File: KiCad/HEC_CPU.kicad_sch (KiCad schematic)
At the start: 19 parts, among them J3 Conn_02x05_Odd_Even, SW2 SW_Push, U1 Z80CPU, U16 74LS32, U20 74LS574, U21 74LS574, U22 74LS02, U23 74LS74, U34 74LS393, U36 74LS574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

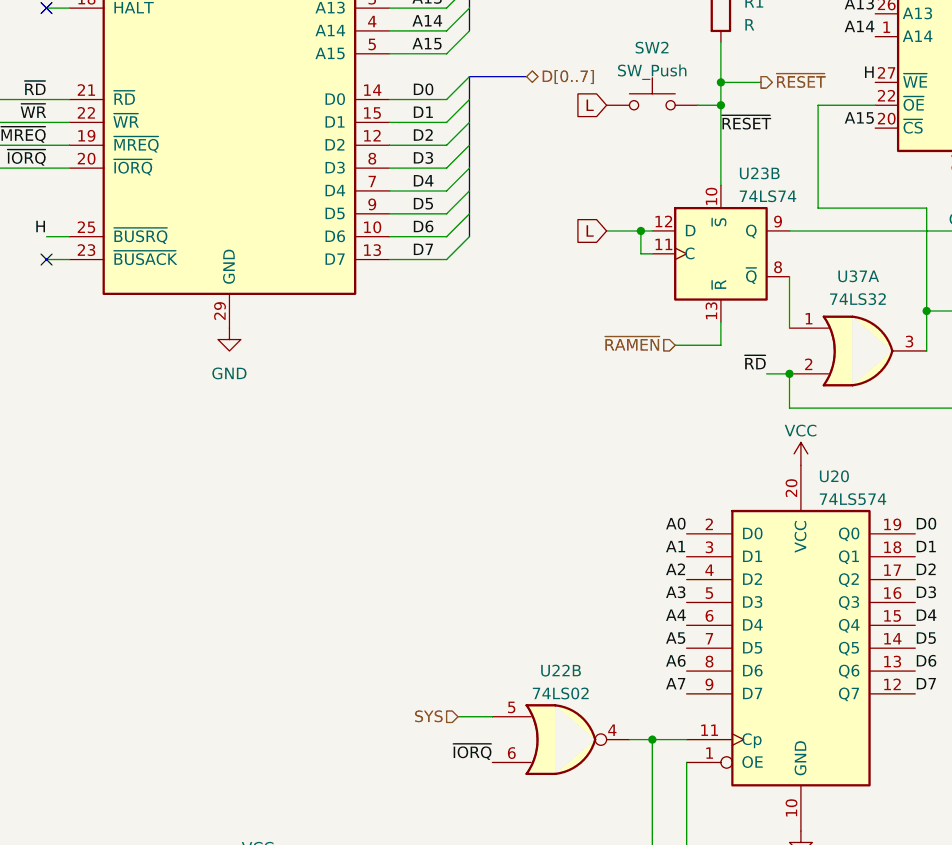
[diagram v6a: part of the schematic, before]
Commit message: Updated layout
Updated the layout of PCB. Chips on the board in this version might be in their final position.
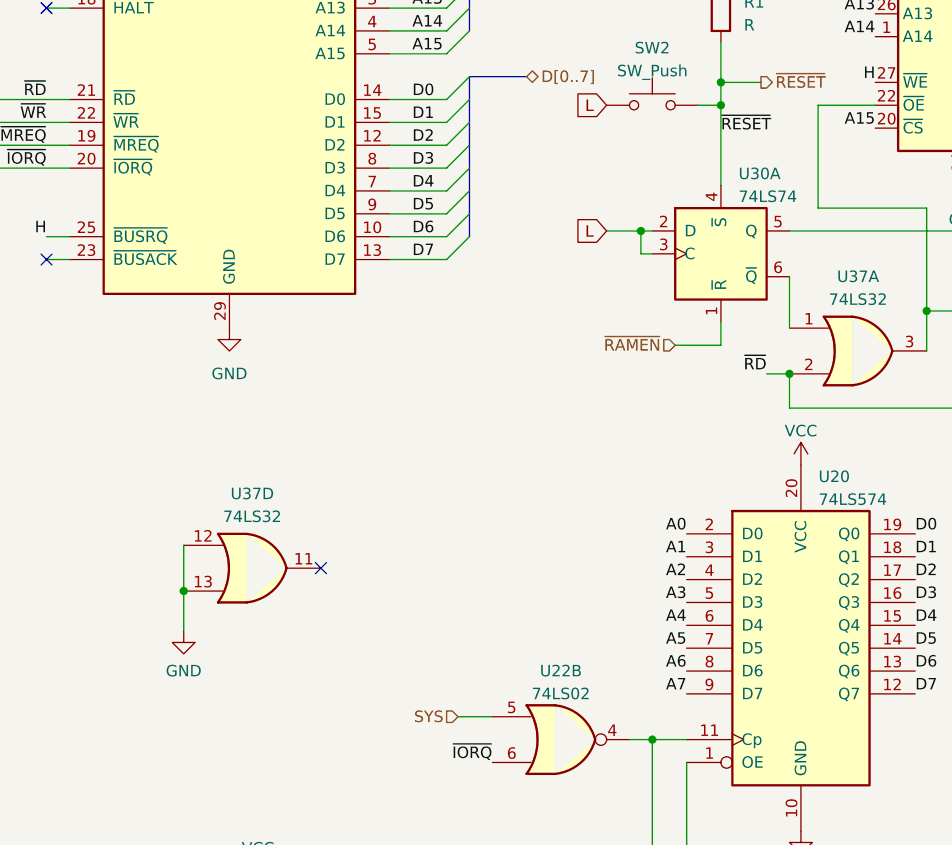
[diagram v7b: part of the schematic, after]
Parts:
- removed U23: 74LS74, Package_DIP:DIP-14_W7.62mm_Socket, symbol 74xx:74LS74
- added U30: 74LS74, Package_DIP:DIP-14_W7.62mm_Socket, symbol 74xx:74LS74
- added unit 4 of U37
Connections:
- net GND: now also U37.12, U37.13
- net L: now also U30.2 (D), U30.3 (C)
- net ~{RAMEN}: now also U30.1 (~{R})
- net ~{RESET}: now also U30.4 (~{S})
- net at U37.1: now also U30.6 (~{Q})
- net at U37.4: now also U30.5 (Q)
- no-connect marks 4 -> 5
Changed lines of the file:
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@@
   (junction (at 101.6 67.945) (diameter 0) (color 0 0 0 0)
+  )
+  (junction (at 41.91 121.92) (diameter 0) (color 0 0 0 0)
   )
   (junction (at 92.71 81.915) (diameter 0) (color 0 0 0 0)
@@
   (no_connect (at 26.67 85.09))
   (no_connect (at 192.405 40.64))
+  (no_connect (at 57.15 119.38))
   (bus_entry (at 71.12 62.23) (size 2.54 -2.54)
     (stroke (width 0) (type default))
@@
     (stroke (width 0) (type default))
   )
+  (wire (pts (xy 41.91 116.84) (xy 41.91 121.92))
+    (stroke (width 0) (type default))
+  )
   (wire (pts (xy 101.6 65.405) (xy 106.045 65.405))
     (stroke (width 0) (type default))
@@
   )
   (wire (pts (xy 280.67 30.48) (xy 278.13 30.48))
+    (stroke (width 0) (type default))
+  )
+  (wire (pts (xy 41.91 121.92) (xy 41.91 126.365))
     (stroke (width 0) (type default))
   )
@@
         (path "/87935374-b60a-4f41-99da-94b76103dd77/73a0c68b-1e42-4c0d-ae31-b1a96d0648bb"
           (reference "#PWR027") (unit 1)
+        )
+      )
+    )
+  )
+  (symbol (lib_id "74xx:74LS32") (at 49.53 119.38 0) (unit 4)
+    (in_bom yes) (on_board yes) (dnp no) (fields_autoplaced)
+    (property "Reference" "U37" (at 49.53 111.125 0)
+      (effects (font (size 1.27 1.27)))
+    )
+    (property "Value" "74LS32" (at 49.53 113.665 0)
+      (effects (font (size 1.27 1.27)))
+    )
+    (property "Footprint" "Package_DIP:DIP-14_W7.62mm_Socket" (at 49.53 119.38 0)
+      (effects (font (size 1.27 1.27)) hide)
+    )
+    (property "Datasheet" "http://www.ti.com/lit/gpn/sn74LS32" (at 49.53 119.38 0)
+      (effects (font (size 1.27 1.27)) hide)
+    )
+    (pin "1")
+    (pin "2")
+    (pin "3")
+    (pin "4")
+    (pin "5")
+    (pin "6")
+    (pin "10")
+    (pin "8")
+    (pin "9")
+    (pin "11")
+    (pin "12")
+    (pin "13")
+    (pin "14")
+    (pin "7")
+    (instances
+      (project "HEC1"
+        (path "/87935374-b60a-4f41-99da-94b76103dd77/73a0c68b-1e42-4c0d-ae31-b1a96d0648bb"
+          (reference "U37") (unit 4)
+        )
+        (path "/87935374-b60a-4f41-99da-94b76103dd77"
+          (reference "U37") (unit 4)
+        )
+        (path "/87935374-b60a-4f41-99da-94b76103dd77/8e836f45-562c-4e39-882e-9c8153296a93"
+          (reference "U37") (unit 4)
         )
       )
@@
     )
   )
+  (symbol (lib_id "74xx:74LS74") (at 101.6 84.455 0) (unit 1)
+    (in_bom yes) (on_board yes) (dnp no) (fields_autoplaced)
+    (property "Reference" "U30" (at 103.5559 75.565 0)
+      (effects (font (size 1.27 1.27)) (justify left))
+    )
+    (property "Value" "74LS74" (at 103.5559 78.105 0)
+      (effects (font (size 1.27 1.27)) (justify left))
+    )
+    (property "Footprint" "Package_DIP:DIP-14_W7.62mm_Socket" (at 101.6 84.455 0)
+      (effects (font (size 1.27 1.27)) hide)
+    )
+    (property "Datasheet" "74xx/74hc_hct74.pdf" (at 101.6 84.455 0)
+      (effects (font (size 1.27 1.27)) hide)
+    )
+    (pin "1")
+    (pin "2")
+    (pin "3")
+    (pin "4")
+    (pin "5")
+    (pin "6")
+    (pin "10")
+    (pin "11")
+    (pin "12")
+    (pin "13")
+    (pin "8")
+    (pin "9")
+    (pin "14")
+    (pin "7")
+    (instances
+      (project "HEC1"
+        (path "/87935374-b60a-4f41-99da-94b76103dd77/2930b625-d6a3-4a7f-9d41-a454efcef99d"
+          (reference "U30") (unit 1)
+        )
+        (path "/87935374-b60a-4f41-99da-94b76103dd77/73a0c68b-1e42-4c0d-ae31-b1a96d0648bb"
+          (reference "U30") (unit 1)
+        )
+      )
+    )
+  )
   (symbol (lib_id "power:VCC") (at 101.6 53.34 0) (unit 1)
     (in_bom yes) (on_board yes) (dnp no) (fields_autoplaced)
@@
     )
   )
-  (symbol (lib_id "74xx:74LS74") (at 101.6 84.455 0) (unit 2)
-    (in_bom yes) (on_board yes) (dnp no) (fields_autoplaced)
-    (property "Reference" "U23" (at 103.5559 75.565 0)
-      (effects (font (size 1.27 1.27)) (justify left))
-    )
-    (property "Value" "74LS74" (at 103.5559 78.105 0)
-      (effects (font (size 1.27 1.27)) (justify left))
-    )
-    (property "Footprint" "Package_DIP:DIP-14_W7.62mm_Socket" (at 101.6 84.455 0)
-      (effects (font (size 1.27 1.27)) hide)
-    )
-    (property "Datasheet" "74xx/74hc_hct74.pdf" (at 101.6 84.455 0)
-      (effects (font (size 1.27 1.27)) hide)
-    )
-    (pin "1")
-    (pin "2")
-    (pin "3")
-    (pin "4")
-    (pin "5")
-    (pin "6")
-    (pin "10")
-    (pin "11")
-    (pin "12")
-    (pin "13")
-    (pin "8")
-    (pin "9")
-    (pin "14")
-    (pin "7")
-    (instances
-      (project "HEC1"
-        (path "/87935374-b60a-4f41-99da-94b76103dd77/73a0c68b-1e42-4c0d-ae31-b1a96d0648bb"
-          (reference "U23") (unit 2)
-        )
-        (path "/87935374-b60a-4f41-99da-94b76103dd77/2930b625-d6a3-4a7f-9d41-a454efcef99d"
-          (reference "U23") (unit 2)
-        )
-      )
-    )
-  )
   (symbol (lib_id "74xx:74LS32") (at 114.3 170.18 0) (unit 3) (convert 2)
     (in_bom yes) (on_board yes) (dnp no) (fields_autoplaced)
@@
         )
       )
+    )
+  )
+  (symbol (lib_id "power:GND") (at 41.91 126.365 0) (unit 1)
+    (in_bom yes) (on_board yes) (dnp no) (fields_autoplaced)
+    (property "Reference" "#PWR0128" (at 41.91 132.715 0)
+      (effects (font (size 1.27 1.27)) hide)
+    )
+    (property "Value" "GND" (at 41.91 130.81 0)
+      (effects (font (size 1.27 1.27)))
+    )
+    (property "Footprint" "" (at 41.91 126.365 0)
+      (effects (font (size 1.27 1.27)) hide)
+    )
+    (property "Datasheet" "" (at 41.91 126.365 0)
+      (effects (font (size 1.27 1.27)) hide)
+    )
+    (pin "1")
+    (instances
+      (project "HEC1"
+        (path "/87935374-b60a-4f41-99da-94b76103dd77/73a0c68b-1e42-4c0d-ae31-b1a96d0648bb"
+          (reference "#PWR0128") (unit 1)
+        )
+      )

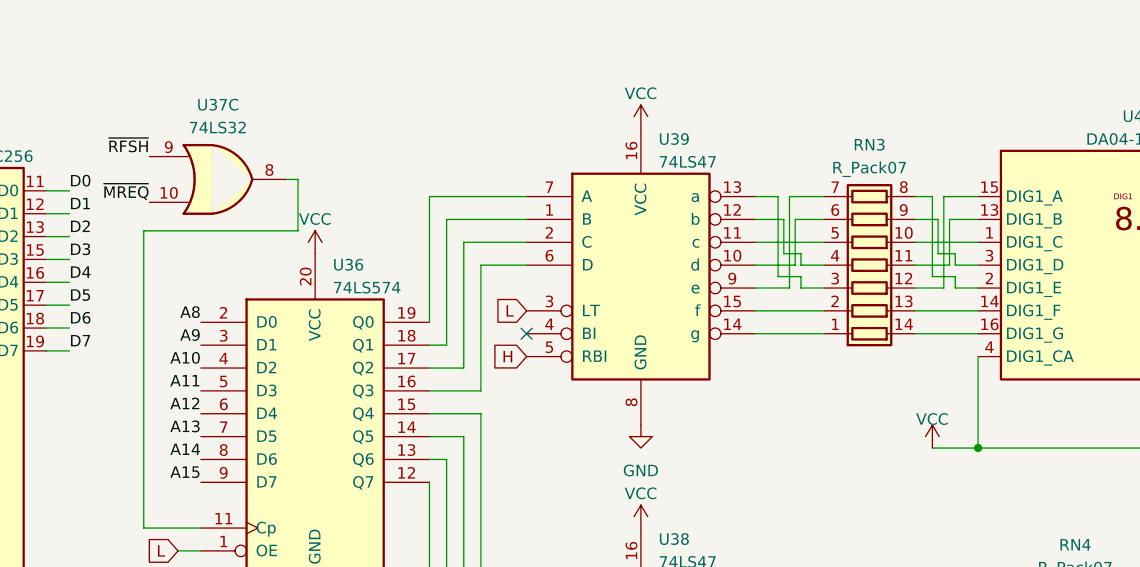
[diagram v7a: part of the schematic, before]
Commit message: Exchange RI and NX pins on bus driver
A mistake is found in the schematic: the RI and NX bits are exchanged on the 74245 bus driver chip. The mistake has been corrected. This change is significant since it changes the (non-existent) software programming model. More playing around with the layout.
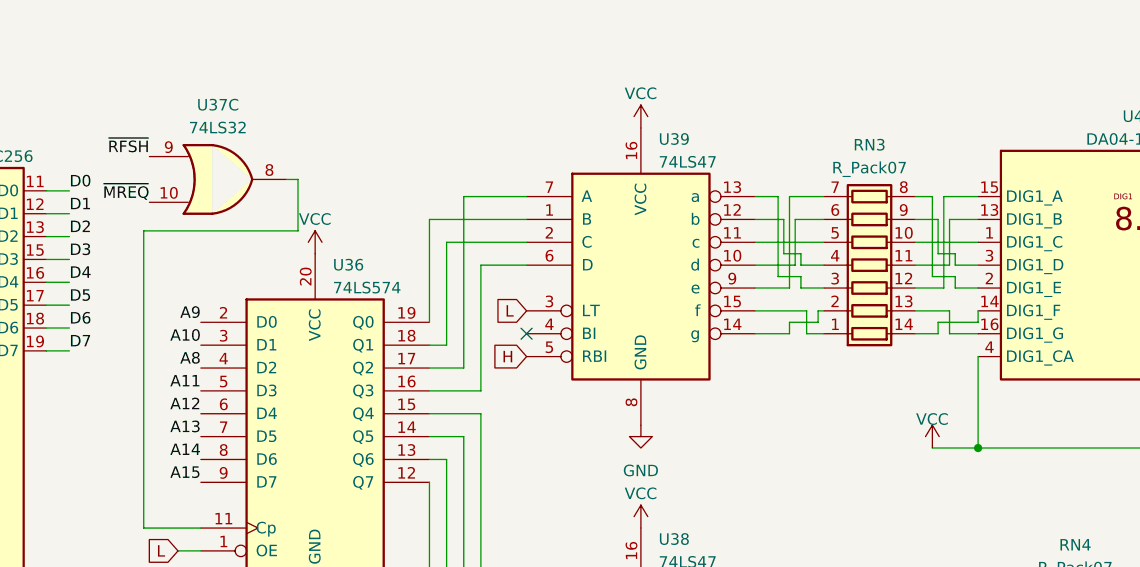
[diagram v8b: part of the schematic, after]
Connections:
- net A10: now also U36.3 (D1); no longer U36.4 (D2)
- net A8: now also U36.4 (D2); no longer U36.2 (D0)
- net A9: now also U36.2 (D0); no longer U36.3 (D1)
- net at U40.14 (DIG1_F): now also RN3.14 (R1.2); no longer RN3.13 (R2.2)
- net at U40.16 (DIG1_G): now also RN3.13 (R2.2); no longer RN3.14 (R1.2)
- net at U36.17 (Q2): now also U39.7 (A); no longer U39.2 (C)
- net at U36.18 (Q1): now also U39.2 (C); no longer U39.1 (B)
- net at U36.19 (Q0): now also U39.1 (B); no longer U39.7 (A)
- net at RN3.1 (R1.1): now also U39.15 (f); no longer U39.14 (g)
- net at RN3.2 (R2.1): now also U39.14 (g); no longer U39.15 (f)
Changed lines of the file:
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@@
+    (stroke (width 0) (type default))
+  )
+  (wire (pts (xy 238.125 40.64) (xy 238.125 39.37))
     (stroke (width 0) (type default))
   )
@@
     (stroke (width 0) (type default))
   )
-  (wire (pts (xy 183.515 27.94) (xy 192.405 27.94))
+  (wire (pts (xy 181.61 27.94) (xy 192.405 27.94))
     (stroke (width 0) (type default))
   )
@@
     (stroke (width 0) (type default))
   )
-  (wire (pts (xy 185.42 44.45) (xy 185.42 30.48))
-    (stroke (width 0) (type default))
-  )
   (wire (pts (xy 240.03 31.75) (xy 240.03 33.02))
     (stroke (width 0) (type default))
@@
     (stroke (width 0) (type default))
   )
+  (wire (pts (xy 239.395 38.1) (xy 235.585 38.1))
+    (stroke (width 0) (type default))
+  )
   (bus (pts (xy 73.66 21.59) (xy 73.66 19.05))
     (stroke (width 0) (type default))
@@
     (stroke (width 0) (type default))
   )
-  (wire (pts (xy 235.585 40.64) (xy 242.57 40.64))
-    (stroke (width 0) (type default))
-  )
   (wire (pts (xy 64.77 59.69) (xy 71.12 59.69))
     (stroke (width 0) (type default))
@@
     (stroke (width 0) (type default))
   )
+  (wire (pts (xy 239.395 40.64) (xy 239.395 38.1))
+    (stroke (width 0) (type default))
+  )
   (wire (pts (xy 238.76 35.56) (xy 235.585 35.56))
     (stroke (width 0) (type default))
@@
     (stroke (width 0) (type default))
   )
+  (wire (pts (xy 185.42 25.4) (xy 185.42 44.45))
+    (stroke (width 0) (type default))
+  )
   (wire (pts (xy 26.67 57.15) (xy 29.21 57.15))
     (stroke (width 0) (type default))
@@
     (stroke (width 0) (type default))
   )
-  (wire (pts (xy 235.585 38.1) (xy 242.57 38.1))
-    (stroke (width 0) (type default))
-  )
   (wire (pts (xy 227.965 78.74) (xy 227.965 80.01))
     (stroke (width 0) (type default))
@@
     (stroke (width 0) (type default))
   )
-  (wire (pts (xy 217.805 38.1) (xy 225.425 38.1))
-    (stroke (width 0) (type default))
-  )
   (wire (pts (xy 92.71 81.915) (xy 93.98 81.915))
     (stroke (width 0) (type default))
@@
     (stroke (width 0) (type default))
   )
+  (wire (pts (xy 238.125 39.37) (xy 242.57 39.37))
+    (stroke (width 0) (type default))
+  )
   (wire (pts (xy 93.98 138.43) (xy 97.79 138.43))
     (stroke (width 0) (type default))
@@
     (stroke (width 0) (type default))
   )
+  (wire (pts (xy 217.805 38.1) (xy 223.52 38.1))
+    (stroke (width 0) (type default))
+  )
   (wire (pts (xy 237.49 25.4) (xy 237.49 34.29))
     (stroke (width 0) (type default))
@@
     (stroke (width 0) (type default))
   )
+  (wire (pts (xy 242.57 40.64) (xy 239.395 40.64))
+    (stroke (width 0) (type default))
+  )
   (wire (pts (xy 167.005 23.495) (xy 167.005 29.21))
     (stroke (width 0) (type default))
   )
+  (wire (pts (xy 224.79 38.1) (xy 225.425 38.1))
+    (stroke (width 0) (type default))
+  )
   (wire (pts (xy 124.46 90.805) (xy 128.27 90.805))
     (stroke (width 0) (type default))
@@
     (stroke (width 0) (type default))
   )
+  (wire (pts (xy 223.52 38.1) (xy 223.52 40.64))
+    (stroke (width 0) (type default))
+  )
   (wire (pts (xy 244.475 153.67) (xy 250.19 153.67))
     (stroke (width 0) (type default))
@@
     (stroke (width 0) (type default))
   )
+  (wire (pts (xy 217.805 40.64) (xy 221.615 40.64))
+    (stroke (width 0) (type default))
+  )
   (wire (pts (xy 222.25 72.39) (xy 222.25 76.2))
     (stroke (width 0) (type default))
@@
     (stroke (width 0) (type default))
   )
+  (wire (pts (xy 223.52 40.64) (xy 225.425 40.64))
+    (stroke (width 0) (type default))
+  )
   (wire (pts (xy 217.805 25.4) (xy 220.345 25.4))
     (stroke (width 0) (type default))
   )
+  (wire (pts (xy 235.585 40.64) (xy 238.125 40.64))
+    (stroke (width 0) (type default))
+  )
   (wire (pts (xy 262.89 153.67) (xy 262.89 156.21))
     (stroke (width 0) (type default))
@@
     (stroke (width 0) (type default))
   )
+  (wire (pts (xy 224.79 39.37) (xy 224.79 38.1))
+    (stroke (width 0) (type default))
+  )
   (wire (pts (xy 222.885 31.75) (xy 222.885 33.02))
     (stroke (width 0) (type default))
@@
     (stroke (width 0) (type default))
   )
+  (wire (pts (xy 242.57 39.37) (xy 242.57 38.1))
+    (stroke (width 0) (type default))
+  )
   (wire (pts (xy 112.395 79.375) (xy 124.46 79.375))
     (stroke (width 0) (type default))
@@
     (stroke (width 0) (type default))
   )
-  (wire (pts (xy 181.61 25.4) (xy 181.61 39.37))
-    (stroke (width 0) (type default))
-  )
   (wire (pts (xy 280.67 74.93) (xy 280.67 30.48))
     (stroke (width 0) (type default))
   )
-  (wire (pts (xy 217.805 40.64) (xy 225.425 40.64))
-    (stroke (width 0) (type default))
-  )
   (wire (pts (xy 20.32 74.93) (xy 29.21 74.93))
     (stroke (width 0) (type default))
@@
     (stroke (width 0) (type default))
   )
+  (wire (pts (xy 221.615 39.37) (xy 224.79 39.37))
+    (stroke (width 0) (type default))
+  )
   (bus (pts (xy 73.66 19.05) (xy 82.55 19.05))
     (stroke (width 0) (type default))
@@
     (stroke (width 0) (type default))
   )
+  (wire (pts (xy 221.615 40.64) (xy 221.615 39.37))
+    (stroke (width 0) (type default))
+  )
   (wire (pts (xy 139.7 101.6) (xy 109.22 101.6))
     (stroke (width 0) (type default))
@@
     (stroke (width 0) (type default))
   )
-  (wire (pts (xy 192.405 25.4) (xy 181.61 25.4))
+  (wire (pts (xy 192.405 25.4) (xy 185.42 25.4))
     (stroke (width 0) (type default))
   )
@@
     (stroke (width 0) (type default))
   )
-  (wire (pts (xy 185.42 30.48) (xy 192.405 30.48))
-    (stroke (width 0) (type default))
-  )
   (wire (pts (xy 235.585 27.94) (xy 238.125 27.94))
     (stroke (width 0) (type default))
@@
     (stroke (width 0) (type default))
   )
-  (wire (pts (xy 183.515 41.91) (xy 183.515 27.94))
+  (wire (pts (xy 183.515 30.48) (xy 192.405 30.48))
+    (stroke (width 0) (type default))
+  )
+  (wire (pts (xy 183.515 41.91) (xy 183.515 30.48))
     (stroke (width 0) (type default))
   )
@@
   )
   (wire (pts (xy 185.42 72.39) (xy 192.405 72.39))
+    (stroke (width 0) (type default))
+  )
+  (wire (pts (xy 181.61 27.94) (xy 181.61 39.37))
     (stroke (width 0) (type default))
   )
@@
     (effects (font (size 1.27 1.27)) (justify left bottom))
   )
-  (label "A9" (at 156.21 41.91 180) (fields_autoplaced)
+  (label "A9" (at 156.21 39.37 180) (fields_autoplaced)
     (effects (font (size 1.27 1.27)) (justify right bottom))
   )
@@
     (effects (font (size 1.27 1.27)) (justify right bottom))
   )
-  (label "A10" (at 156.21 44.45 180) (fields_autoplaced)
+  (label "A10" (at 156.21 41.91 180) (fields_autoplaced)
     (effects (font (size 1.27 1.27)) (justify right bottom))
   )
@@
     (effects (font (size 1.27 1.27)) (justify left bottom))
   )
-  (label "A8" (at 156.21 39.37 180) (fields_autoplaced)
-    (effects (font (size 1.27 1.27)) (justify right bottom))
-  )
+  (label "A8" (at 156.21 44.45 180) (fields_autoplaced)
+    (effects (font (size 1.27 1.27)) (justify right bottom))
+  )
